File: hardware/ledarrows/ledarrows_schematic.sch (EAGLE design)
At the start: 35 parts, among them CN1 1X4-BIG, IC1 7805T, T1 2N2222, T2 2N2222, T3 2N2222, T4 2N2222

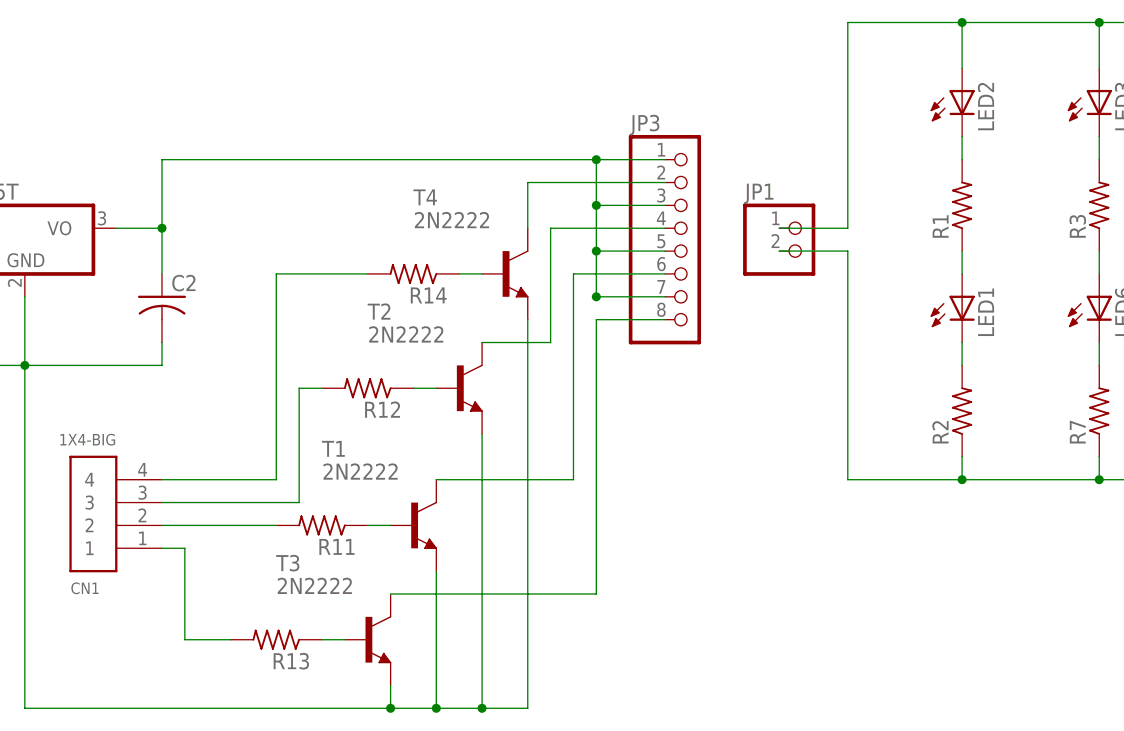
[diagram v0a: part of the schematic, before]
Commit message: Updating schematics of servos and ledarrows to include the db15 connector used to interface outside of the electronics enclosure.
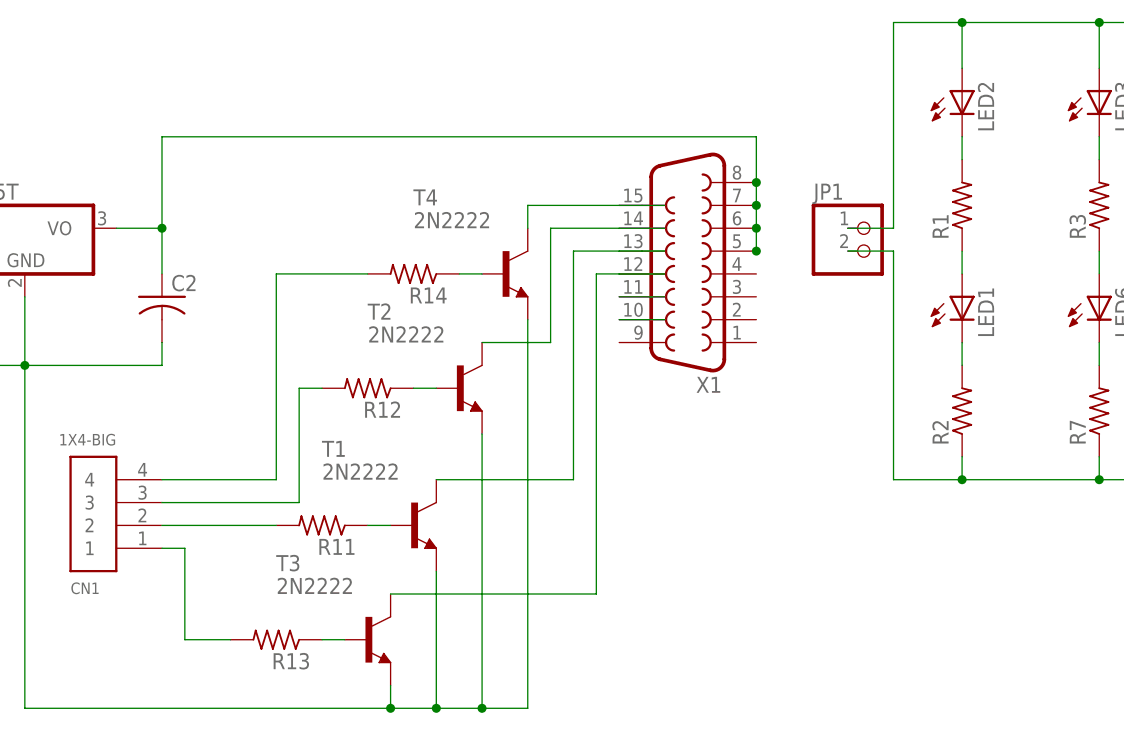
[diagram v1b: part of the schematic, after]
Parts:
- removed JP3: (no value), adafruit:PINHD-1X8CLEANBIG
- added X1: (no value), adafruit:F15H
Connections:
- removed net N$32: JP3.2, T4.C
- removed net N$33: JP3.4, T2.C
- new net N$31: X1.11
- new net N$34: T4.C, X1.15
- new net N$36: X1.10
- new net N$38: T2.C, X1.14
- net N$22: now also X1.5, X1.6, X1.7, X1.8; no longer JP3.1, JP3.3, JP3.5, JP3.7
- net N$25: now also X1.13; no longer JP3.6
- net N$30: now also X1.12; no longer JP3.8
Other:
- moved on the sheet: JP1
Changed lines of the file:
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@@
 <part name="T4" library="adafruit" deviceset="2N2222" device=""/>
 <part name="R14" library="adafruit" deviceset="R-US_" device="0204/7"/>
-<part name="JP3" library="adafruit" deviceset="PINHD-1X8" device="CLEANBIG"/>
+<part name="X1" library="adafruit" deviceset="F15" device="H"/>
 </parts>
 <sheets>
@@
 <instance part="T1" gate="G$1" x="-35.56" y="30.48"/>
 <instance part="R11" gate="G$1" x="-45.72" y="30.48" rot="R180"/>
-<instance part="JP1" gate="G$1" x="7.62" y="60.96"/>
+<instance part="JP1" gate="G$1" x="15.24" y="60.96"/>
 <instance part="T2" gate="G$1" x="-30.48" y="45.72"/>
 <instance part="R12" gate="G$1" x="-40.64" y="45.72" rot="R180"/>
@@
 <instance part="T4" gate="G$1" x="-25.4" y="58.42"/>
 <instance part="R14" gate="G$1" x="-35.56" y="58.42" rot="R180"/>
-<instance part="JP3" gate="G$1" x="-5.08" y="63.5"/>
+<instance part="X1" gate="-1" x="-5.08" y="58.42" rot="R180"/>
 </instances>
 <busses>
@@
 <wire x1="71.12" y1="86.36" x2="71.12" y2="81.28" width="0.1524" layer="91"/>
 <pinref part="JP1" gate="G$1" pin="1"/>
-<wire x1="5.08" y1="63.5" x2="12.7" y2="63.5" width="0.1524" layer="91"/>
-<wire x1="12.7" y1="63.5" x2="12.7" y2="86.36" width="0.1524" layer="91"/>
-<wire x1="12.7" y1="86.36" x2="25.4" y2="86.36" width="0.1524" layer="91"/>
+<wire x1="12.7" y1="63.5" x2="17.78" y2="63.5" width="0.1524" layer="91"/>
+<wire x1="17.78" y1="63.5" x2="17.78" y2="86.36" width="0.1524" layer="91"/>
+<wire x1="17.78" y1="86.36" x2="25.4" y2="86.36" width="0.1524" layer="91"/>
 <junction x="25.4" y="86.36"/>
 <junction x="40.64" y="86.36"/>
@@
 <wire x1="40.64" y1="38.1" x2="40.64" y2="35.56" width="0.1524" layer="91"/>
 <pinref part="JP1" gate="G$1" pin="2"/>
-<wire x1="5.08" y1="60.96" x2="12.7" y2="60.96" width="0.1524" layer="91"/>
-<wire x1="12.7" y1="60.96" x2="12.7" y2="35.56" width="0.1524" layer="91"/>
-<wire x1="12.7" y1="35.56" x2="25.4" y2="35.56" width="0.1524" layer="91"/>
+<wire x1="12.7" y1="60.96" x2="17.78" y2="60.96" width="0.1524" layer="91"/>
+<wire x1="17.78" y1="60.96" x2="17.78" y2="35.56" width="0.1524" layer="91"/>
+<wire x1="17.78" y1="35.56" x2="25.4" y2="35.56" width="0.1524" layer="91"/>
 <junction x="71.12" y="35.56"/>
 <junction x="55.88" y="35.56"/>
@@
 <net name="N$22" class="0">
 <segment>
-<wire x1="-63.5" y1="71.12" x2="-15.24" y2="71.12" width="0.1524" layer="91"/>
 <pinref part="IC1" gate="A1" pin="VO"/>
-<wire x1="-15.24" y1="71.12" x2="-7.62" y2="71.12" width="0.1524" layer="91"/>
 <wire x1="-68.58" y1="63.5" x2="-63.5" y2="63.5" width="0.1524" layer="91"/>
-<wire x1="-63.5" y1="63.5" x2="-63.5" y2="71.12" width="0.1524" layer="91"/>
+<wire x1="-63.5" y1="63.5" x2="-63.5" y2="73.66" width="0.1524" layer="91"/>
 <wire x1="-63.5" y1="63.5" x2="-63.5" y2="58.42" width="0.1524" layer="91"/>
 <pinref part="C2" gate="G$1" pin="1"/>
 <junction x="-63.5" y="63.5"/>
-<pinref part="JP3" gate="G$1" pin="1"/>
-<wire x1="-15.24" y1="71.12" x2="-15.24" y2="66.04" width="0.1524" layer="91"/>
-<pinref part="JP3" gate="G$1" pin="7"/>
-<wire x1="-15.24" y1="66.04" x2="-15.24" y2="60.96" width="0.1524" layer="91"/>
-<wire x1="-15.24" y1="60.96" x2="-15.24" y2="55.88" width="0.1524" layer="91"/>
-<wire x1="-15.24" y1="55.88" x2="-7.62" y2="55.88" width="0.1524" layer="91"/>
-<pinref part="JP3" gate="G$1" pin="5"/>
-<wire x1="-15.24" y1="60.96" x2="-7.62" y2="60.96" width="0.1524" layer="91"/>
-<wire x1="-15.24" y1="66.04" x2="-7.62" y2="66.04" width="0.1524" layer="91"/>
-<junction x="-15.24" y="71.12"/>
-<junction x="-15.24" y="66.04"/>
-<junction x="-15.24" y="60.96"/>
-<junction x="-15.24" y="55.88"/>
-<pinref part="JP3" gate="G$1" pin="3"/>
+<pinref part="X1" gate="-1" pin="8"/>
+<wire x1="2.54" y1="68.58" x2="2.54" y2="73.66" width="0.1524" layer="91"/>
+<wire x1="2.54" y1="73.66" x2="-63.5" y2="73.66" width="0.1524" layer="91"/>
+<pinref part="X1" gate="-1" pin="5"/>
+<wire x1="2.54" y1="68.58" x2="2.54" y2="66.04" width="0.1524" layer="91"/>
+<junction x="2.54" y="60.96"/>
+<pinref part="X1" gate="-1" pin="6"/>
+<junction x="2.54" y="63.5"/>
+<wire x1="2.54" y1="66.04" x2="2.54" y2="63.5" width="0.1524" layer="91"/>
+<wire x1="2.54" y1="63.5" x2="2.54" y2="60.96" width="0.1524" layer="91"/>
+<pinref part="X1" gate="-1" pin="7"/>
+<junction x="2.54" y="66.04"/>
+<junction x="2.54" y="68.58"/>
 </segment>
 </net>
@@
 </segment>
 </net>
-<net name="N$32" class="0">
-<segment>
+<net name="N$25" class="0">
+<segment>
+<pinref part="T1" gate="G$1" pin="C"/>
+<wire x1="-33.02" y1="35.56" x2="-17.78" y2="35.56" width="0.1524" layer="91"/>
+<wire x1="-17.78" y1="35.56" x2="-17.78" y2="60.96" width="0.1524" layer="91"/>
+<wire x1="-12.7" y1="60.96" x2="-10.16" y2="60.96" width="0.1524" layer="91"/>
+<pinref part="X1" gate="-1" pin="13"/>
+<wire x1="-10.16" y1="60.96" x2="-7.62" y2="60.96" width="0.1524" layer="91"/>
+<wire x1="-17.78" y1="60.96" x2="-12.7" y2="60.96" width="0.1524" layer="91"/>
+</segment>
+</net>
+<net name="N$30" class="0">
+<segment>
+<pinref part="T3" gate="G$1" pin="C"/>
+<wire x1="-38.1" y1="22.86" x2="-15.24" y2="22.86" width="0.1524" layer="91"/>
+<wire x1="-15.24" y1="22.86" x2="-15.24" y2="58.42" width="0.1524" layer="91"/>
+<pinref part="X1" gate="-1" pin="12"/>
+<wire x1="-12.7" y1="58.42" x2="-7.62" y2="58.42" width="0.1524" layer="91"/>
+<wire x1="-15.24" y1="58.42" x2="-12.7" y2="58.42" width="0.1524" layer="91"/>
+</segment>
+</net>
+<net name="N$31" class="0">
+<segment>
+<wire x1="-12.7" y1="55.88" x2="-7.62" y2="55.88" width="0.1524" layer="91"/>
+<pinref part="X1" gate="-1" pin="11"/>
+</segment>
+</net>
+<net name="N$34" class="0">
+<segment>
+<pinref part="X1" gate="-1" pin="15"/>
+<wire x1="-12.7" y1="66.04" x2="-10.16" y2="66.04" width="0.1524" layer="91"/>
 <pinref part="T4" gate="G$1" pin="C"/>
-<wire x1="-22.86" y1="63.5" x2="-22.86" y2="68.58" width="0.1524" layer="91"/>
-<pinref part="JP3" gate="G$1" pin="2"/>
-<wire x1="-22.86" y1="68.58" x2="-7.62" y2="68.58" width="0.1524" layer="91"/>
-</segment>
-</net>
-<net name="N$33" class="0">
-<segment>
+<wire x1="-10.16" y1="66.04" x2="-7.62" y2="66.04" width="0.1524" layer="91"/>
+<wire x1="-22.86" y1="63.5" x2="-22.86" y2="66.04" width="0.1524" layer="91"/>
+<wire x1="-22.86" y1="66.04" x2="-12.7" y2="66.04" width="0.1524" layer="91"/>
+</segment>
+</net>
+<net name="N$36" class="0">
+<segment>
+<pinref part="X1" gate="-1" pin="10"/>
+<wire x1="-12.7" y1="53.34" x2="-7.62" y2="53.34" width="0.1524" layer="91"/>
+</segment>
+</net>
+<net name="N$38" class="0">
+<segment>
+<pinref part="X1" gate="-1" pin="14"/>
+<wire x1="-12.7" y1="63.5" x2="-7.62" y2="63.5" width="0.1524" layer="91"/>
 <pinref part="T2" gate="G$1" pin="C"/>
 <wire x1="-27.94" y1="50.8" x2="-20.32" y2="50.8" width="0.1524" layer="91"/>
 <wire x1="-20.32" y1="50.8" x2="-20.32" y2="63.5" width="0.1524" layer="91"/>
-<pinref part="JP3" gate="G$1" pin="4"/>
-<wire x1="-20.32" y1="63.5" x2="-7.62" y2="63.5" width="0.1524" layer="91"/>
-</segment>
-</net>
-<net name="N$25" class="0">
-<segment>
-<pinref part="T1" gate="G$1" pin="C"/>
-<wire x1="-33.02" y1="35.56" x2="-17.78" y2="35.56" width="0.1524" layer="91"/>
-<wire x1="-17.78" y1="35.56" x2="-17.78" y2="58.42" width="0.1524" layer="91"/>
-<pinref part="JP3" gate="G$1" pin="6"/>
-<wire x1="-17.78" y1="58.42" x2="-7.62" y2="58.42" width="0.1524" layer="91"/>
-</segment>
-</net>
-<net name="N$30" class="0">
-<segment>
-<pinref part="T3" gate="G$1" pin="C"/>
-<wire x1="-38.1" y1="22.86" x2="-15.24" y2="22.86" width="0.1524" layer="91"/>
-<wire x1="-15.24" y1="22.86" x2="-15.24" y2="53.34" width="0.1524" layer="91"/>
-<pinref part="JP3" gate="G$1" pin="8"/>
-<wire x1="-15.24" y1="53.34" x2="-7.62" y2="53.34" width="0.1524" layer="91"/>
-</segment>
-</net>
+<wire x1="-12.7" y1="63.5" x2="-20.32" y2="63.5" width="0.1524" layer="91"/>
+</segment>
+</net>

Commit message: Schematics updates: Adding a shield schematic file for the microcontroller board header connector and power breakdown. Adding page border to existing schematics. Adding a few component values. Updating the display schematic to use common cathode 7 segment.
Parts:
- removed R3, R4, R5, R6: (no value), adafruit:R-US_0204/7
- added LED11: (no value), adafruit:LED3MM
- C1: value (none) -> 0.33 uF
- C2: value (none) -> 0.1 uF
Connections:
- removed net N$12: LED3.C, R3.2
- removed net N$13: LED2.C, R1.2
- removed net N$14: LED1.A, R1.1
- removed net N$17: LED4.C, R4.2
- net N$10: now also LED10.A, LED7.C; no longer LED8.A, R4.1
- net N$11: now also LED11.C, R1.2; no longer LED6.A, R3.1
- net N$18: now also R1.1
- net N$2: now also LED1.A, LED2.C; no longer LED10.A, R6.1
- net N$3: now also LED3.C, LED6.A; no longer LED7.C, R6.2
- net N$4: now also LED11.A
- net N$6: now also LED4.C, LED8.A; no longer LED5.C, R5.2
- net N$7: no longer R5.1
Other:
- note added: "Temporary DB15 pinout"
- moved on the sheet: LED1, LED10, LED6, LED8, LED9, R1, R10, R2, R7, R8, R9

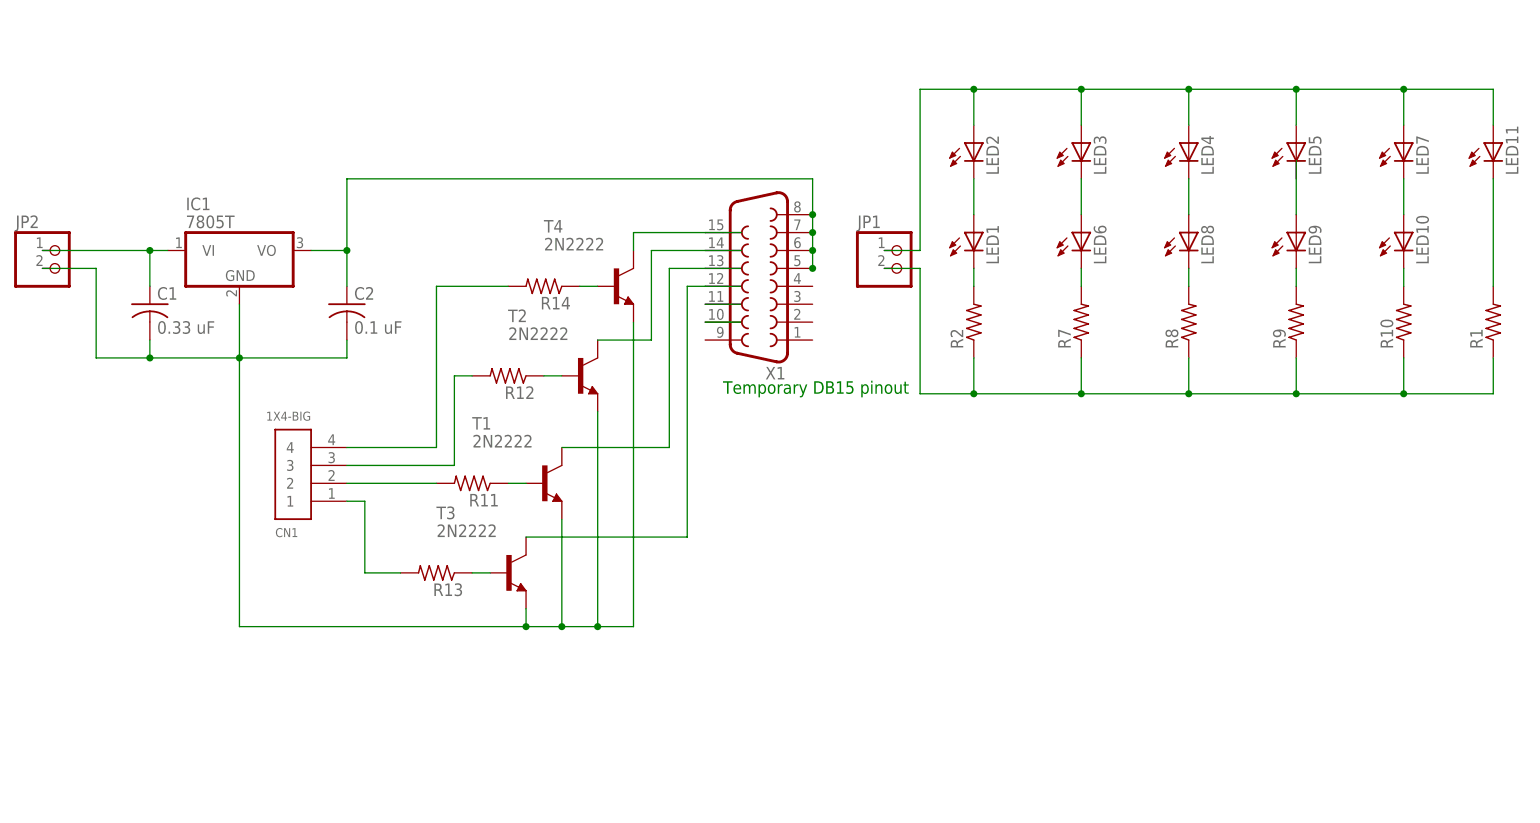
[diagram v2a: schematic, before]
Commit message: Updating the schematics to include A5 frames and complete some component values. Also adding the arduino shield symbol to the shield schematic.
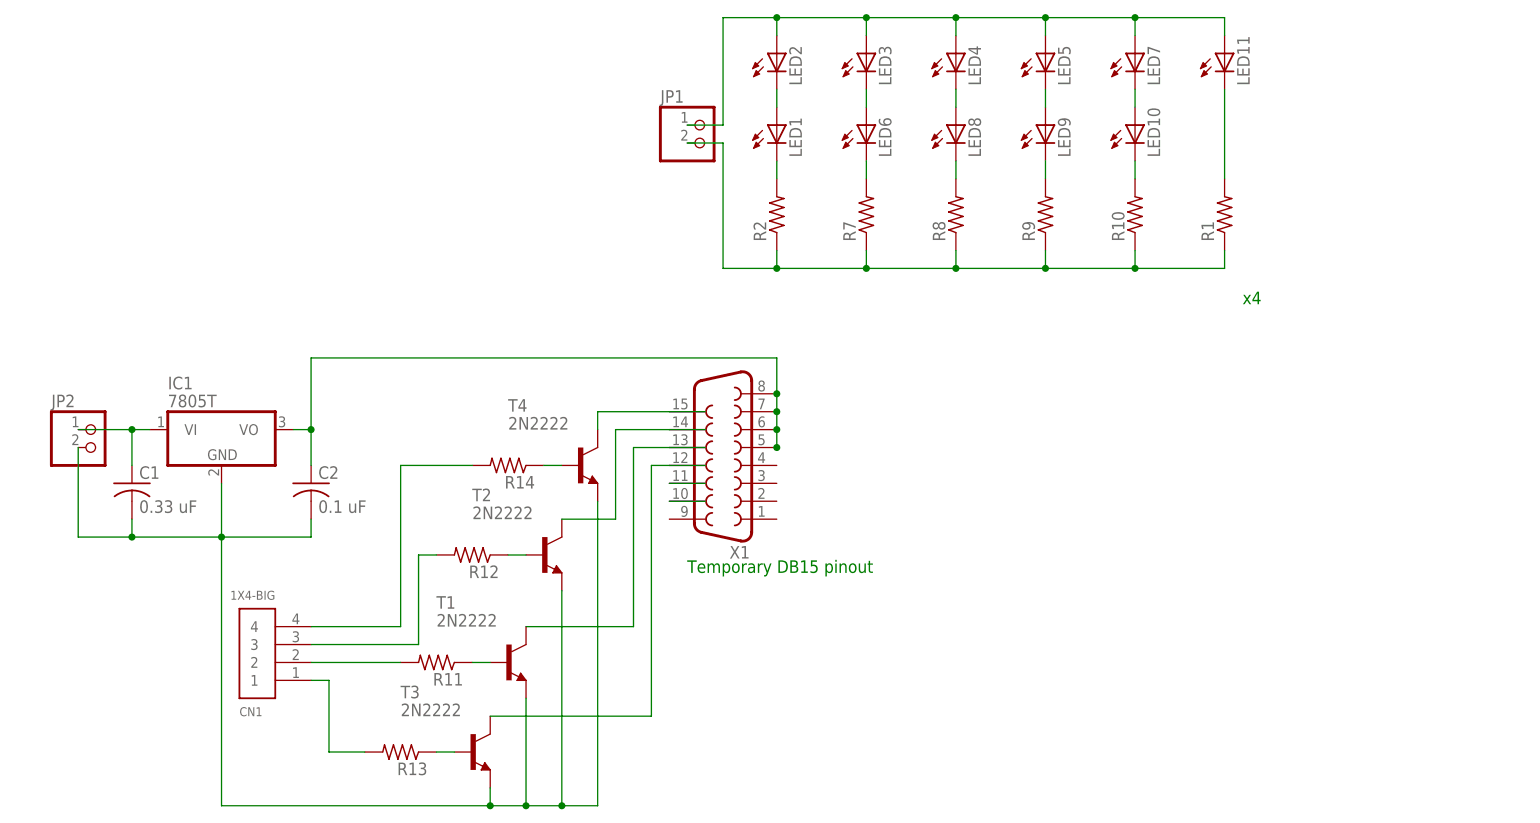
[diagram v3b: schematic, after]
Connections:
- net N$29: now also JP2.2
- net N$7: now also LED5.C
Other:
- note added: "x4"
- moved on the sheet: C1, C2, CN1, IC1, JP1, JP2, LED1, LED10, LED11, LED2, LED3, LED4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

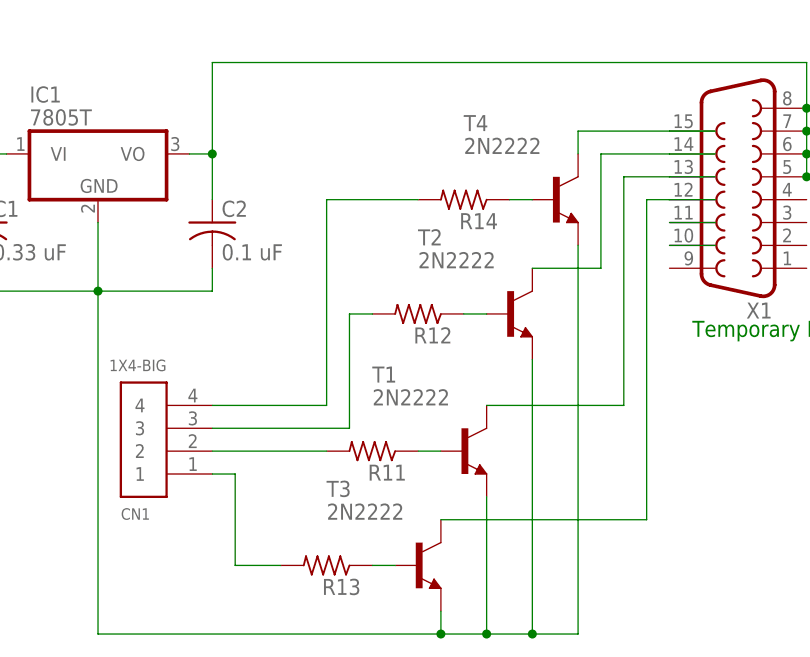
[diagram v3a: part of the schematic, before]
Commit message: updating resistor values in schematics
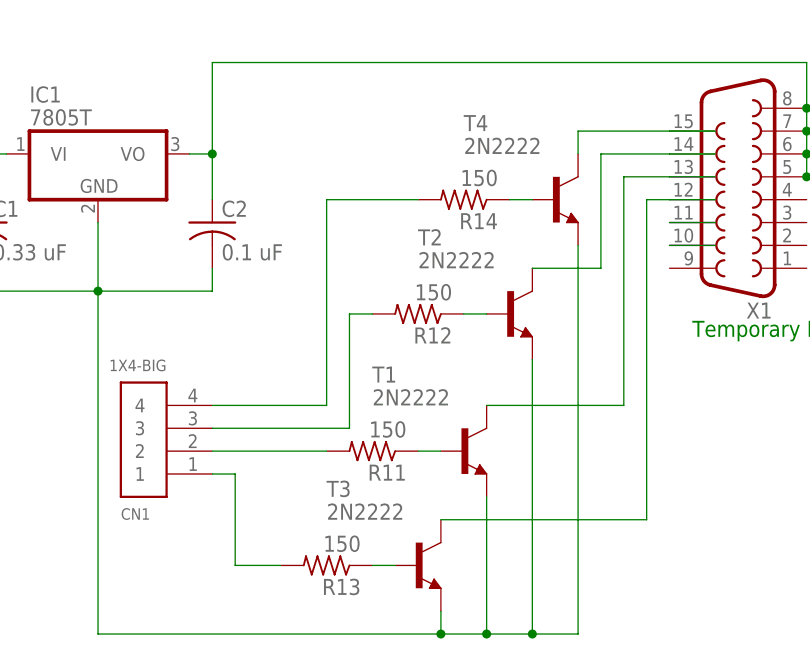
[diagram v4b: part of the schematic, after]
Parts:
- R11, R12, R13, R14: value (none) -> 150
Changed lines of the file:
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@@
 <part name="R10" library="adafruit" deviceset="R-US_" device="0204/7"/>
 <part name="T1" library="adafruit" deviceset="2N2222" device=""/>
-<part name="R11" library="adafruit" deviceset="R-US_" device="0204/7"/>
+<part name="R11" library="adafruit" deviceset="R-US_" device="0204/7" value="150"/>
 <part name="JP1" library="pinhead" deviceset="PINHD-1X2" device=""/>
 <part name="T2" library="adafruit" deviceset="2N2222" device=""/>
-<part name="R12" library="adafruit" deviceset="R-US_" device="0204/7"/>
+<part name="R12" library="adafruit" deviceset="R-US_" device="0204/7" value="150"/>
 <part name="IC1" library="adafruit" deviceset="78*" device="T" technology="05"/>
 <part name="C1" library="adafruit" deviceset="C-US" device="025-050X050" value="0.33 uF"/>
@@
 <part name="JP2" library="pinhead" deviceset="PINHD-1X2" device=""/>
 <part name="T3" library="adafruit" deviceset="2N2222" device=""/>
-<part name="R13" library="adafruit" deviceset="R-US_" device="0204/7"/>
+<part name="R13" library="adafruit" deviceset="R-US_" device="0204/7" value="150"/>
 <part name="T4" library="adafruit" deviceset="2N2222" device=""/>
-<part name="R14" library="adafruit" deviceset="R-US_" device="0204/7"/>
+<part name="R14" library="adafruit" deviceset="R-US_" device="0204/7" value="150"/>
 <part name="X1" library="adafruit" deviceset="F15" device="H"/>
 <part name="LED11" library="adafruit" deviceset="LED" device="3MM"/>
